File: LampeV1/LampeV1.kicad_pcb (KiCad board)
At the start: 2 copper layers, 15 parts, among them J1 Screw_Terminal_01x06, J2 Screw_Terminal_01x04, J3 Conn_01x05_Male, J4 Conn_01x04_Male, Q7 BT136-500, U1 ESP32-S2-DevKitM, U2 STA301a, U3 EL817, U4 MOC3020M, U5 R-78B5.0-2.0

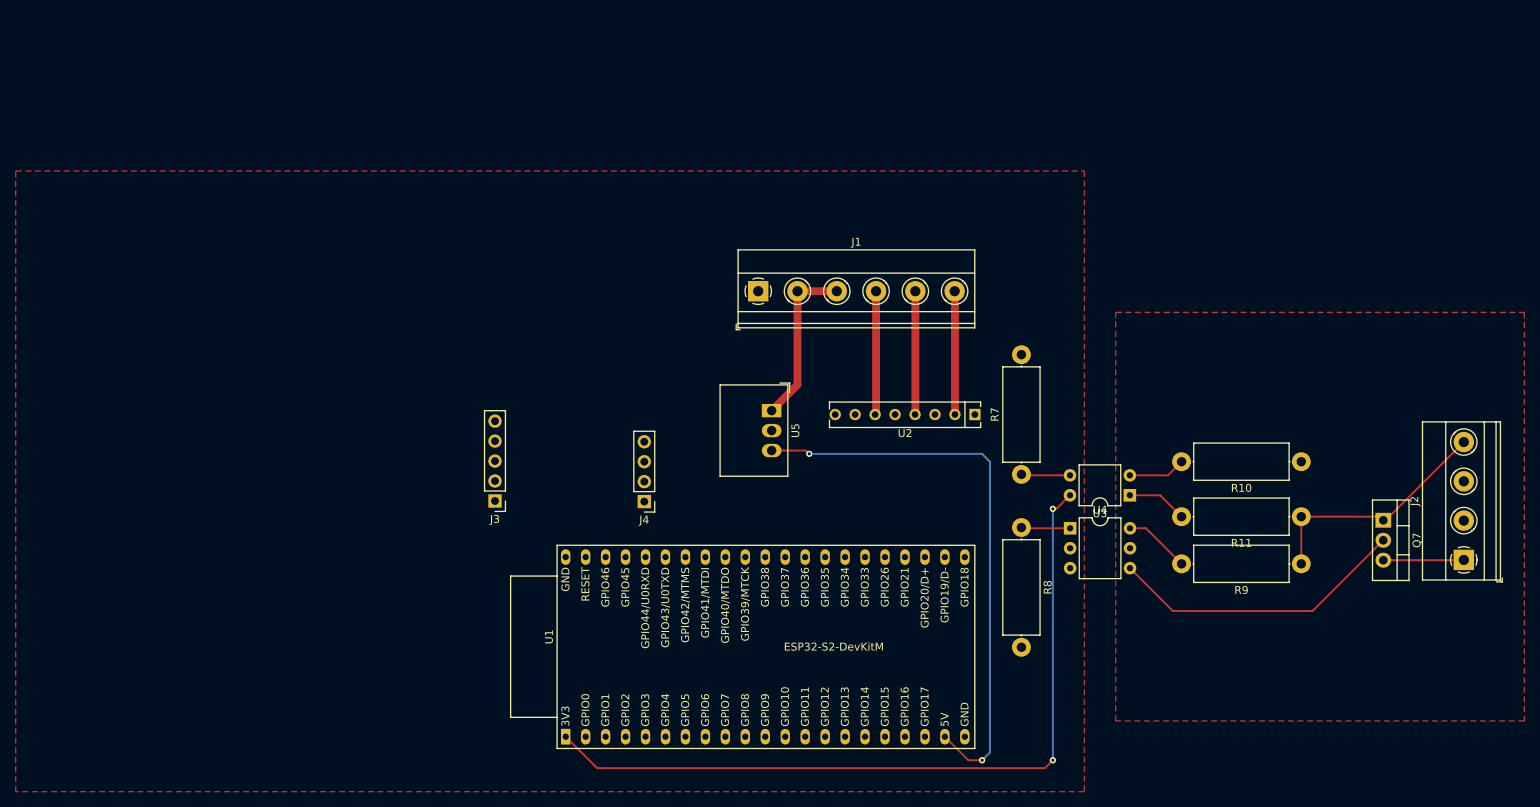
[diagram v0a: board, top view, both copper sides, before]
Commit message: added case
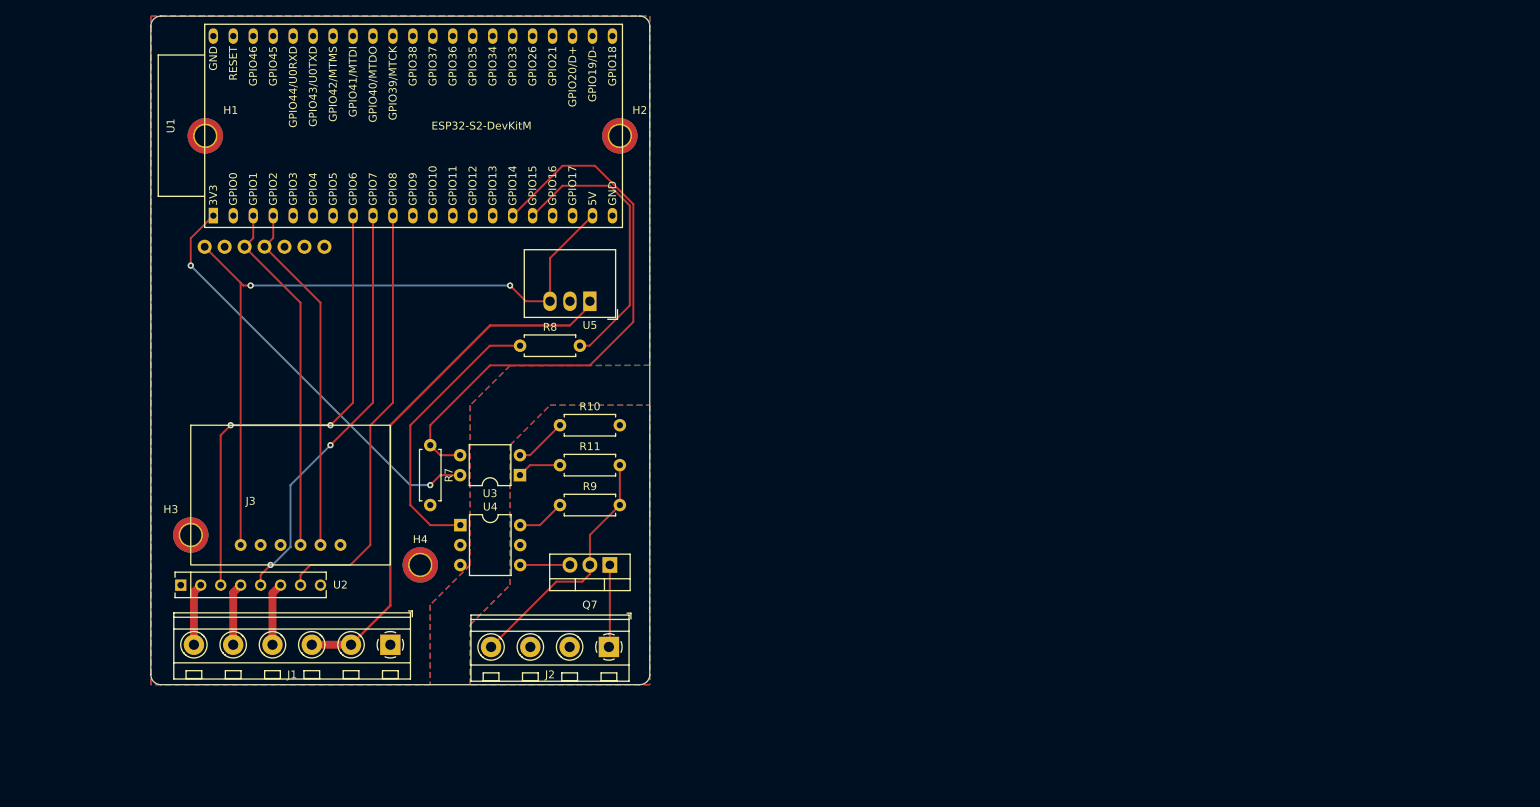
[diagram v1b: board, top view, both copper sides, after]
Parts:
- added H1: MountingHole_Pad, MountingHole:MountingHole_2.7mm_M2.5_ISO14580_Pad_TopBottom, F.Cu at (83.1, 49.5)
- added H2: MountingHole_Pad, MountingHole:MountingHole_2.7mm_M2.5_ISO14580_Pad_TopBottom, F.Cu at (135.9, 49.5)
- added H3: MountingHole_Pad, MountingHole:MountingHole_2.7mm_M2.5_ISO14580_Pad_TopBottom, F.Cu at (81.3, 100.3)
- added H4: MountingHole_Pad, MountingHole:MountingHole_2.7mm_M2.5_ISO14580_Pad_TopBottom, F.Cu at (110.5, 104.1)
- J1: footprint TerminalBlock_Phoenix:TerminalBlock_Phoenix_MKDS-1,5-6_1x06_P5.00mm_Horizontal -> TerminalBlock_MetzConnect:TerminalBlock_MetzConnect_Type094_RT03506HBLU_1x06_P5.00mm_Horizontal
- J2: footprint TerminalBlock_Phoenix:TerminalBlock_Phoenix_MKDS-1,5-4_1x04_P5.00mm_Horizontal -> TerminalBlock_MetzConnect:TerminalBlock_MetzConnect_Type094_RT03504HBLU_1x04_P5.00mm_Horizontal
- J3: footprint Connector_PinHeader_2.54mm:PinHeader_1x05_P2.54mm_Vertical -> manual:LTR390
- J4: value Conn_01x04_Male -> Conn_01x07_Male; footprint Connector_PinHeader_2.54mm:PinHeader_1x04_P2.54mm_Vertical -> manual:scd30
- R10, R11, R7, R8, R9: footprint Resistor_THT:R_Axial_DIN0414_L11.9mm_D4.5mm_P15.24mm_Horizontal -> Resistor_THT:R_Axial_DIN0207_L6.3mm_D2.5mm_P7.62mm_Horizontal
- U3: value EL817 -> LTV-814
- moved J2 109.4 mm to (134.5, 114.6), turned to 180 degrees
- moved U2 103.4 mm to (80.0, 106.7), turned to 0 degrees
- moved Q7 98.6 mm to (134.6, 104.1), turned to 180 degrees
- moved R9 94.6 mm to (128.3, 96.5), turned to 0 degrees
- moved R11 94.6 mm to (128.3, 91.4), turned to 0 degrees
- moved R10 94.5 mm to (128.3, 86.4), turned to 0 degrees
- moved U1 80.1 mm to (84.2, 59.7)
- moved U3 77.7 mm to (123.2, 92.7)
- moved U4 77.6 mm to (115.6, 99.1)
- moved R7 75.3 mm to (111.8, 88.9), turned to -90 degrees
- moved R8 67.9 mm to (123.2, 76.2), turned to 0 degrees
- moved J4 66.6 mm to (81.6, 62.2)
- moved J1 64.9 mm to (106.7, 114.3), turned to 180 degrees
- moved J3 31.1 mm to (88.9, 96.5), turned to 0 degrees
- moved U5 27.0 mm to (132.1, 70.6), turned to 180 degrees
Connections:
- Q7 pad 1: AC -> Net-(J2-Pad1)
- Q7 pad 2: Net-(Q7-Pad2) -> AC
- Q7 pad 3: Net-(J2-Pad1) -> Net-(Q7-Pad3)
- R10 pad 1: GNDA -> Net-(R10-Pad1)
- R10 pad 2: Net-(R10-Pad2) -> GNDA
- R11 pad 1: AC -> Net-(R11-Pad1)
- R11 pad 2: Net-(R11-Pad2) -> AC
- R9 pad 1: AC -> Net-(R9-Pad1)
- R9 pad 2: Net-(R9-Pad2) -> AC
- U1 pad 10: unconnected-(U1-Pad10) -> Net-(U1-Pad10)
- U1 pad 16: unconnected-(U1-Pad16) -> Net-(R7-Pad1)
- U1 pad 17: unconnected-(U1-Pad17) -> Net-(R8-Pad2)
- U1 pad 26: /scl -> unconnected-(U1-Pad26)
- U1 pad 27: /sda -> unconnected-(U1-Pad27)
- U1 pad 28: Net-(R7-Pad1) -> unconnected-(U1-Pad28)
- U1 pad 29: Net-(R8-Pad2) -> unconnected-(U1-Pad29)
- U1 pad 3: unconnected-(U1-Pad3) -> /scl
- U1 pad 30: Net-(U1-Pad30) -> unconnected-(U1-Pad30)
- U1 pad 31: Net-(U1-Pad31) -> unconnected-(U1-Pad31)
- U1 pad 32: Net-(U1-Pad32) -> unconnected-(U1-Pad32)
- U1 pad 4: unconnected-(U1-Pad4) -> /sda
- U1 pad 8: unconnected-(U1-Pad8) -> Net-(U1-Pad8)
- U1 pad 9: unconnected-(U1-Pad9) -> Net-(U1-Pad9)
- U2 pad 3: Net-(U1-Pad30) -> Net-(U1-Pad8)
- U2 pad 5: Net-(U1-Pad31) -> Net-(U1-Pad9)
- U2 pad 7: Net-(U1-Pad32) -> Net-(U1-Pad10)
- U3 pad 1: Net-(R11-Pad2) -> Net-(R11-Pad1)
- U3 pad 2: Net-(R10-Pad2) -> Net-(R10-Pad1)
- U4 pad 4: Net-(Q7-Pad2) -> Net-(Q7-Pad3)
- U4 pad 6: Net-(R9-Pad2) -> Net-(R9-Pad1)
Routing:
- net Net-(R7-Pad1): track 6.23 -> 73.2 mm
- net Net-(U1-Pad8): track 0.00 -> 61.4 mm, vias 0 -> 2
- net Net-(U1-Pad10): track 0.00 -> 54.9 mm
- net Net-(U1-Pad9): track 0.00 -> 53.1 mm, vias 0 -> 2
- net +12V: track 21.6 -> 67.3 mm
- net /sda: track 0.00 -> 45.3 mm
- net /scl: track 0.00 -> 45.3 mm
- net +3V3: track 99.0 -> 53.9 mm
- net Net-(Q7-Pad2): track 38.2 -> 0.00 mm
- net Net-(R8-Pad2): track 0.00 -> 36.2 mm
- net Net-(R8-Pad1): track 6.24 -> 35.8 mm
- net +5V: track 72.8 -> 93.3 mm
- net Net-(R9-Pad2): track 8.43 -> 0.00 mm
- net Net-(J1-Pad6): track 15.7 -> 7.95 mm
- net Net-(J1-Pad4): track 15.7 -> 8.02 mm
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- added copper zone on B.Cu, net GND
- added copper zone on B.Cu, net GNDA
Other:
- board outline added: 63.5 x 85.1 mm
